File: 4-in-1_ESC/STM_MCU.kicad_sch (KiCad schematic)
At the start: 11 parts, among them U12 STM32G071GBU6

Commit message: update
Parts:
- added R108, R112: 470R, Resistor_SMD:R_0201_0603Metric, symbol Device:R_Small_US
- C71, C80, C81, C83: footprint Capacitor_SMD:C_0402_1005Metric -> Capacitor_SMD:C_0201_0603Metric
- D13: value LED_Small -> XL-0201UGC; footprint (none) -> LED_SMD:LED_0201_0603Metric; LCSC_Part_Number (none) -> C3646922
- R100, R104, R85: footprint Resistor_SMD:R_0402_1005Metric -> Resistor_SMD:R_0201_0603Metric
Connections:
- net DSHOT_RX: now also R112.1; no longer U12.24 (PB4)
- net KISS_TELEM: now also R108.2; no longer U12.26 (PB6)
- new net: R112.2, U12.24 (PB4)
- new net: R108.1, U12.26 (PB6)

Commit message: changes
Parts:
- removed R108, R112: 470R, Resistor_SMD:R_0201_0603Metric, symbol Device:R_Small_US
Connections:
- net DSHOT_RX: now also U12.24 (PB4)
- net KISS_TELEM: now also U12.26 (PB6)
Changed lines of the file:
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@@
 		)
 	)
+	(text_box "VERIFY THIS^^"
+		(exclude_from_sim no)
+		(at 45.72 142.24 0)
+		(size 33.02 10.0806)
+		(margins 0.9525 0.9525 0.9525 0.9525)
+		(stroke
+			(width 0)
+			(type solid)
+		)
+		(fill
+			(type color)
+			(color 255 229 191 1)
+		)
+		(effects
+			(font
+				(size 2.54 2.54)
+				(color 255 0 0 1)
+			)
+			(justify left top)
+		)
+	)
 	(text_box "SIGNALS & SENSORS\nPin     Function           Signal\nPA2     TIM2_CH3 (AF2)     DShot RX ← FC\nPA2     USART2_TX (AF1)    BDShot TX → FC (runtime switch)\nPA0     ADC_IN0            Phase current (shunt amp)\nPA1     ADC_IN1            Battery voltage (divider)\nPA4     ADC_IN4            NTC temperature\nPB6     USART1_TX (AF0)    Telemetry → FC\nPA13    SWDIO (AF0)        Debug probe\nPA14    SWCLK (AF0)        Debug probe"
 		(exclude_from_sim no)
@@
 		)
 	)
+	(text_box "PICK COMPONENT"
+		(exclude_from_sim no)
+		(at 237.49 53.4194 0)
+		(size 33.02 10.0806)
+		(margins 0.9525 0.9525 0.9525 0.9525)
+		(stroke
+			(width 0)
+			(type solid)
+		)
+		(fill
+			(type color)
+			(color 255 229 191 1)
+		)
+		(effects
+			(font
+				(size 2.54 2.54)
+				(color 255 0 0 1)
+			)
+			(justify left top)
+		)
+	)
 	(junction
 		(at 160.02 64.77)
@@
 	(wire
 		(pts
-			(xy 222.25 106.68) (xy 224.79 106.68)
-		)
-		(stroke
-			(width 0)
-			(type default)
-		)
-	)
-	(wire
-		(pts
 			(xy 119.38 59.69) (xy 129.54 59.69)
 		)
@@
 	(wire
 		(pts
-			(xy 207.01 111.76) (xy 217.17 111.76)
+			(xy 207.01 111.76) (xy 215.9 111.76)
 		)
 		(stroke
@@
 	(wire
 		(pts
-			(xy 207.01 123.19) (xy 213.36 123.19)
+			(xy 207.01 123.19) (xy 215.9 123.19)
 		)
 		(stroke
@@
 	(wire
 		(pts
-			(xy 207.01 120.65) (xy 213.36 120.65)
+			(xy 207.01 120.65) (xy 215.9 120.65)
 		)
 		(stroke
@@
 	(wire
 		(pts
-			(xy 207.01 106.68) (xy 217.17 106.68)
+			(xy 207.01 106.68) (xy 215.9 106.68)
 		)
 		(stroke
@@
 	(wire
 		(pts
-			(xy 222.25 111.76) (xy 224.79 111.76)
-		)
-		(stroke
-			(width 0)
-			(type default)
-		)
-	)
-	(wire
-		(pts
 			(xy 152.4 64.77) (xy 160.02 64.77)
 		)
@@
 	(hierarchical_label "KISS_TELEM"
 		(shape output)
-		(at 224.79 106.68 0)
+		(at 215.9 106.68 0)
 		(effects
 			(font
@@
 	(hierarchical_label "SWCLK"
 		(shape output)
-		(at 213.36 120.65 0)
+		(at 215.9 120.65 0)
 		(effects
 			(font
@@
 	(hierarchical_label "DSHOT_RX"
 		(shape output)
-		(at 224.79 111.76 0)
+		(at 215.9 111.76 0)
 		(effects
 			(font
@@
 	(hierarchical_label "SWDIO"
 		(shape output)
-		(at 213.36 123.19 0)
+		(at 215.9 123.19 0)
 		(effects
 			(font
@@
 	)
 	(symbol
-		(lib_id "Device:R_Small_US")
-		(at 219.71 111.76 270)
-		(unit 1)
-		(body_style 1)
-		(exclude_from_sim no)
-		(in_bom yes)
-		(on_board yes)
-		(in_pos_files yes)
-		(dnp no)
-		(property "Reference" "R112"
-			(at 217.424 114.3 90)
-			(show_name no)
-			(do_not_autoplace no)
-			(effects
-				(font
-					(size 1.27 1.27)
-				)
-				(justify left)
-			)
-		)
-		(property "Value" "470R"
-			(at 217.424 116.84 90)
-			(show_name no)
-			(do_not_autoplace no)
-			(effects
-				(font
-					(size 1.27 1.27)
-				)
-				(justify left)
-			)
-		)
-		(property "Footprint" "Resistor_SMD:R_0201_0603Metric"
-			(at 219.71 111.76 0)
-			(hide yes)
-			(show_name no)
-			(do_not_autoplace no)
-			(effects
-				(font
-					(size 1.27 1.27)
-				)
-			)
-		)
-		(property "Datasheet" ""
-			(at 219.71 111.76 0)
-			(hide yes)
-			(show_name no)
-			(do_not_autoplace no)
-			(effects
-				(font
-					(size 1.27 1.27)
-				)
-			)
-		)
-		(property "Description" "Resistor, small US symbol"
-			(at 219.71 111.76 0)
-			(hide yes)
-			(show_name no)
-			(do_not_autoplace no)
-			(effects
-				(font
-					(size 1.27 1.27)
-				)
-			)
-		)
-		(pin "2"
-		)
-		(pin "1"
-		)
-		(instances
-			(project "4-in-1_ESC"
-				(path "/885456b2-b92d-459f-a061-5f970a420f96/6564a7b2-a052-4d05-afff-891845561909"
-					(reference "R115")
-					(unit 1)
-				)
-				(path "/885456b2-b92d-459f-a061-5f970a420f96/773805d5-0506-47cb-968e-b54ab0ee2e7c"
-					(reference "R114")
-					(unit 1)
-				)
-				(path "/885456b2-b92d-459f-a061-5f970a420f96/77e6c738-31a1-455c-884f-364258be6798"
-					(reference "R113")
-					(unit 1)
-				)
-				(path "/885456b2-b92d-459f-a061-5f970a420f96/be886d77-ef71-4773-9408-03142af02e9b"
-					(reference "R112")
-					(unit 1)
-				)
-			)
-		)
-	)
-	(symbol
 		(lib_id "Device:C_Small")
 		(at 160.02 69.85 0)
@@
 					(unit 1)
 				)
-			)
-		)
-	)
-	(symbol
-		(lib_id "Device:R_Small_US")
-		(at 219.71 106.68 90)
-		(unit 1)
-		(body_style 1)
-		(exclude_from_sim no)
-		(in_bom yes)
-		(on_board yes)
-		(in_pos_files yes)
-		(dnp no)
-		(property "Reference" "R108"
-			(at 217.424 101.6 90)
-			(show_name no)
-			(do_not_autoplace no)
-			(effects
-				(font
-					(size 1.27 1.27)
-				)
-				(justify right)
-			)
-		)
-		(property "Value" "470R"
-			(at 217.424 104.14 90)
-			(show_name no)
-			(do_not_autoplace no)
-			(effects
-				(font
-					(size 1.27 1.27)
-				)
-				(justify right)
-			)
-		)
-		(property "Footprint" "Resistor_SMD:R_0201_0603Metric"
-			(at 219.71 106.68 0)
-			(hide yes)
-			(show_name no)
-			(do_not_autoplace no)
-			(effects
-				(font
-					(size 1.27 1.27)
-				)
-			)
-		)
-		(property "Datasheet" ""
-			(at 219.71 106.68 0)
-			(hide yes)
-			(show_name no)
-			(do_not_autoplace no)
-			(effects
-				(font
-					(size 1.27 1.27)
-				)
-			)
-		)
-		(property "Description" "Resistor, small US symbol"
-			(at 219.71 106.68 0)
-			(hide yes)
-			(show_name no)
-			(do_not_autoplace no)
-			(effects
-				(font
-					(size 1.27 1.27)
-				)
-			)
-		)
-		(pin "2"
-		)
-		(pin "1"
-		)
-		(instances
-			(project "4-in-1_ESC"
-				(path "/885456b2-b92d-459f-a061-5f970a420f96/6564a7b2-a052-4d05-afff-891845561909"
-					(reference "R111")
-					(unit 1)
-				)
-				(path "/885456b2-b92d-459f-a061-5f970a420f96/773805d5-0506-47cb-968e-b54ab0ee2e7c"
-					(reference "R110")
-					(unit 1)
-				)
-				(path "/885456b2-b92d-459f-a061-5f970a420f96/77e6c738-31a1-455c-884f-364258be6798"
-					(reference "R109")
-					(unit 1)
-				)
-				(path "/885456b2-b92d-459f-a061-5f970a420f96/be886d77-ef71-4773-9408-03142af02e9b"
-					(reference "R108")
-					(unit 1)
-				)

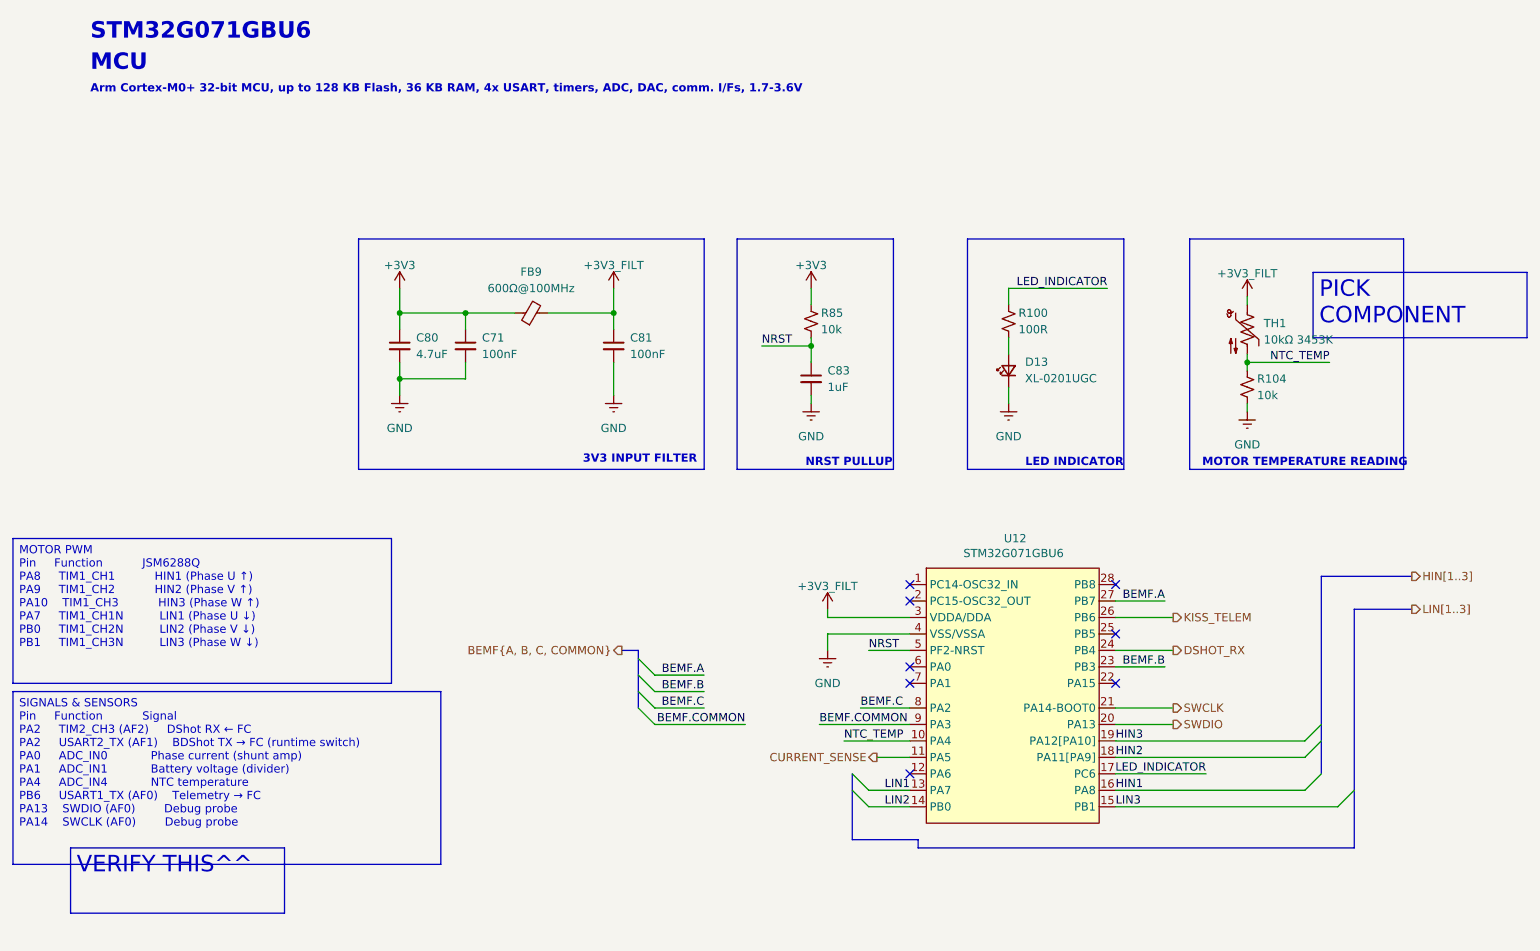
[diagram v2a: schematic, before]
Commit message: Schematic Updates
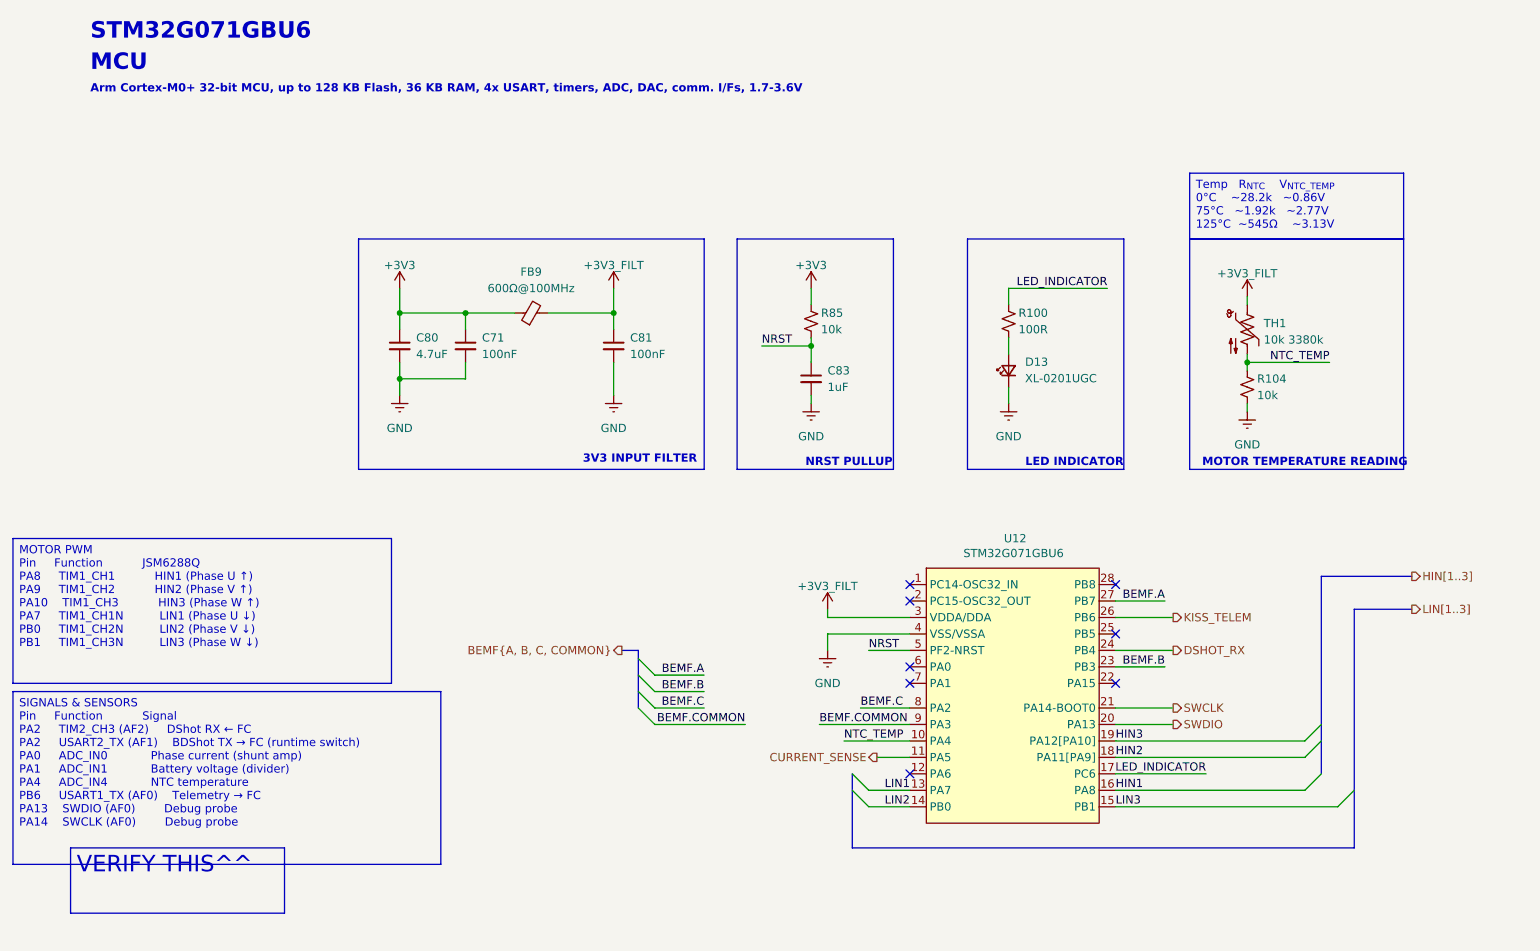
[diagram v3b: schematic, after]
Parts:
- TH1: value 10kΩ 3453K -> 10k 3380k; footprint (none) -> Resistor_SMD:R_0402_1005Metric; LCSC_Part_Number (none) -> C209959
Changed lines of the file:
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@@
 		)
 	)
-	(text_box "SIGNALS & SENSORS\nPin     Function           Signal\nPA2     TIM2_CH3 (AF2)     DShot RX ← FC\nPA2     USART2_TX (AF1)    BDShot TX → FC (runtime switch)\nPA0     ADC_IN0            Phase current (shunt amp)\nPA1     ADC_IN1            Battery voltage (divider)\nPA4     ADC_IN4            NTC temperature\nPB6     USART1_TX (AF0)    Telemetry → FC\nPA13    SWDIO (AF0)        Debug probe\nPA14    SWCLK (AF0)        Debug probe"
+	(text_box "Temp   R_{NTC}    V_{NTC_TEMP}\n0°C    ~28.2k   ~0.86V\n75°C   ~1.92k   ~2.77V\n125°C  ~545Ω    ~3.13V\n"
 		(exclude_from_sim no)
-		(at 36.83 118.11 0)
-		(size 66.04 26.67)
+		(at 218.44 38.1 0)
+		(size 33.02 10.16)
 		(margins 0.9525 0.9525 0.9525 0.9525)
 		(stroke
@@
 		)
 	)
-	(text_box "MOTOR PWM\nPin     Function           JSM6288Q\nPA8     TIM1_CH1           HIN1 (Phase U ↑)\nPA9     TIM1_CH2           HIN2 (Phase V ↑)\nPA10    TIM1_CH3           HIN3 (Phase W ↑)\nPA7     TIM1_CH1N          LIN1 (Phase U ↓)\nPB0     TIM1_CH2N          LIN2 (Phase V ↓)\nPB1     TIM1_CH3N          LIN3 (Phase W ↓)"
+	(text_box "SIGNALS & SENSORS\nPin     Function           Signal\nPA2     TIM2_CH3 (AF2)     DShot RX ← FC\nPA2     USART2_TX (AF1)    BDShot TX → FC (runtime switch)\nPA0     ADC_IN0            Phase current (shunt amp)\nPA1     ADC_IN1            Battery voltage (divider)\nPA4     ADC_IN4            NTC temperature\nPB6     USART1_TX (AF0)    Telemetry → FC\nPA13    SWDIO (AF0)        Debug probe\nPA14    SWCLK (AF0)        Debug probe"
 		(exclude_from_sim no)
-		(at 36.83 94.49 0)
-		(size 58.42 22.35)
+		(at 36.83 118.11 0)
+		(size 66.04 26.67)
 		(margins 0.9525 0.9525 0.9525 0.9525)
 		(stroke
@@
 		)
 	)
-	(text_box "PICK COMPONENT"
+	(text_box "MOTOR PWM\nPin     Function           JSM6288Q\nPA8     TIM1_CH1           HIN1 (Phase U ↑)\nPA9     TIM1_CH2           HIN2 (Phase V ↑)\nPA10    TIM1_CH3           HIN3 (Phase W ↑)\nPA7     TIM1_CH1N          LIN1 (Phase U ↓)\nPB0     TIM1_CH2N          LIN2 (Phase V ↓)\nPB1     TIM1_CH3N          LIN3 (Phase W ↓)"
 		(exclude_from_sim no)
-		(at 237.49 53.4194 0)
-		(size 33.02 10.0806)
+		(at 36.83 94.49 0)
+		(size 58.42 22.35)
 		(margins 0.9525 0.9525 0.9525 0.9525)
 		(stroke
@@
 		)
 		(fill
-			(type color)
-			(color 255 229 191 1)
+			(type none)
 		)
 		(effects
 			(font
-				(size 2.54 2.54)
-				(color 255 0 0 1)
+				(size 1.27 1.27)
 			)
 			(justify left top)
@@
 		)
 	)
-	(bus
-		(pts
-			(xy 176.53 140.97) (xy 176.53 142.24)
-		)
-		(stroke
-			(width 0)
-			(type default)
-		)
-	)
-	(bus
-		(pts
-			(xy 243.84 142.24) (xy 176.53 142.24)
-		)
-		(stroke
-			(width 0)
-			(type default)
-		)
-	)
 	(wire
 		(pts
@@
 	(bus
 		(pts
-			(xy 166.37 140.97) (xy 166.37 130.81)
+			(xy 166.37 142.24) (xy 166.37 130.81)
 		)
 		(stroke
@@
 	(bus
 		(pts
-			(xy 176.53 140.97) (xy 166.37 140.97)
+			(xy 166.37 142.24) (xy 243.84 142.24)
 		)
 		(stroke
@@
 			)
 		)
-		(property "Value" "10kΩ 3453K"
+		(property "Value" "10k 3380k"
 			(at 229.87 63.8174 0)
 			(show_name no)
@@
 			)
 		)
-		(property "Footprint" ""
+		(property "Footprint" "Resistor_SMD:R_0402_1005Metric"
 			(at 227.33 60.96 0)
 			(hide yes)
@@
 			(at 227.33 62.23 0)
 			(hide yes)
+			(show_name no)
+			(do_not_autoplace no)
+			(effects
+				(font
+					(size 1.27 1.27)
+				)
+			)
+		)
+		(property "LCSC_Part_Number" "C209959"
+			(at 227.33 62.23 0)
+			(hide yes)

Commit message: update
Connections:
- net VBAT_SENSE: now reaches U12.12 (PA6)
- no-connect marks 8 -> 7
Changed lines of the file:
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@@
+		)
+	)
+	(text_box "CHANGE PINOUT FOR ROUTING"
+		(exclude_from_sim no)
+		(at 176.53 146.05 0)
+		(size 33.02 10.0806)
+		(margins 0.9525 0.9525 0.9525 0.9525)
+		(stroke
+			(width 0)
+			(type solid)
+		)
+		(fill
+			(type color)
+			(color 255 229 191 1)
+		)
+		(effects
+			(font
+				(size 2.54 2.54)
+				(color 255 0 0 1)
+			)
+			(justify left top)
 		)
 	)
@@
 		(at 207.01 101.6)
 	)
-	(no_connect
-		(at 175.26 130.81)
-	)
 	(bus_entry
 		(at 133.35 113.03)
@@
 	)
 	(bus_entry
-		(at 166.37 133.35)
+		(at 149.86 133.35)
 		(size 2.54 2.54)
 		(stroke
@@
 	)
 	(bus_entry
-		(at 166.37 130.81)
+		(at 149.86 130.81)
 		(size 2.54 2.54)
 		(stroke
@@
 	(wire
 		(pts
-			(xy 168.91 133.35) (xy 175.26 133.35)
+			(xy 152.4 133.35) (xy 175.26 133.35)
+		)
+		(stroke
+			(width 0)
+			(type default)
+		)
+	)
+	(wire
+		(pts
+			(xy 170.18 130.81) (xy 175.26 130.81)
 		)
 		(stroke
@@
 	(bus
 		(pts
-			(xy 166.37 142.24) (xy 166.37 130.81)
+			(xy 149.86 142.24) (xy 149.86 130.81)
 		)
 		(stroke
@@
 	(bus
 		(pts
-			(xy 166.37 142.24) (xy 243.84 142.24)
+			(xy 149.86 142.24) (xy 243.84 142.24)
 		)
 		(stroke
@@
 	(wire
 		(pts
-			(xy 168.91 135.89) (xy 175.26 135.89)
+			(xy 152.4 135.89) (xy 175.26 135.89)
 		)
 		(stroke
@@
 		)
 	)
+	(hierarchical_label "VBAT_SENSE"
+		(shape output)
+		(at 170.18 130.81 180)
+		(effects
+			(font
+				(size 1.27 1.27)
+			)
+			(justify right)
+		)
+	)

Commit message: Update
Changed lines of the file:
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@@
 				(thickness 0.508)
 				(bold yes)
-				(color 255 255 255 1)
+				(color 255 0 0 1)
 			)
 			(justify left)
@@
 				(thickness 0.508)
 				(bold yes)
-				(color 255 255 255 1)
+				(color 255 0 0 1)
 			)
 			(justify left)
@@
 				(thickness 0.508)
 				(bold yes)
-				(color 255 255 255 1)
+				(color 255 0 0 1)
 			)
 			(justify left)
-		)
-	)
-	(text_box "VERIFY THIS^^"
-		(exclude_from_sim no)
-		(at 45.72 142.24 0)
-		(size 33.02 10.0806)
-		(margins 0.9525 0.9525 0.9525 0.9525)
-		(stroke
-			(width 0)
-			(type solid)
-		)
-		(fill
-			(type color)
-			(color 255 229 191 1)
-		)
-		(effects
-			(font
-				(size 2.54 2.54)
-				(color 255 0 0 1)
-			)
-			(justify left top)
 		)
 	)
@@
 			)
 			(justify left top)
-		)
-	)
-	(text_box "CHANGE PINOUT FOR ROUTING"
-		(exclude_from_sim no)
-		(at 176.53 146.05 0)
-		(size 33.02 10.0806)
-		(margins 0.9525 0.9525 0.9525 0.9525)
-		(stroke
-			(width 0)
-			(type solid)
-		)
-		(fill
-			(type color)
-			(color 255 229 191 1)
-		)
-		(effects
-			(font
-				(size 2.54 2.54)
-				(color 255 0 0 1)
-			)
-			(justify left top)
